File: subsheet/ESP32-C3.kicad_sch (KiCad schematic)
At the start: 0 parts

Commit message: Add ESP32-C3 subsheet. SMall corrections
Add and wire up ESP32-C3-Mini on a subsheet, and note down which pins
are used for strapping etc. This will then be replaced with a bare-chip
ESP32-C3 circuit, much like with the existing ESP32-S3 circuit.
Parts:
- added C601: 100nF/50V, Capacitor_SMD:C_0603_1608Metric, symbol Device:C_Small
- added J601: Conn_01x06, Connector_PinSocket_2.54mm:PinSocket_1x06_P2.54mm_Vertical, symbol Connector_Generic:Conn_01x06
- added R601: 10kΩ, Resistor_SMD:R_0603_1608Metric, symbol Device:R_US
- added R602, R603: 100kΩ, Resistor_SMD:R_0603_1608Metric, symbol Device:R_Small_US
- added SW601, SW602: SW_Push, Button_Switch_SMD_custom:SW_PUSHBUTTON_2PIN_SMD_3×4×2.0, symbol Switch:SW_Push
- added U601: ESP32-C3-MINI-1, Espressif:ESP32-C3-MINI-1, symbol Espressif:ESP32-C3-MINI-1
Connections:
- new net +3V3: J601.4 (Pin_4), R601.1, R602.1, R603.1
- new net ESP_EN: C601.1, J601.5 (Pin_5), R601.2, SW602.2, U601.8 (EN/CHIP_PU)
- new net GND: C601.2, J601.1 (Pin_1), SW601.1, SW602.1, U601.1 (GND), U601.11 (GND), U601.14 (GND), U601.2 (GND), U601.36 (GND), U601.37 (GND), U601.38 (GND), U601.39 (GND), U601.40 (GND), U601.41 (GND), U601.42 (GND), U601.43 (GND), U601.44 (GND), U601.45 (GND), U601.46 (GND), U601.47 (GND), U601.48 (GND), U601.49 (GND), U601.50 (GND), U601.51 (GND), U601.52 (GND), U601.53 (GND)
- new net GPIO18/USB_D-: U601.26 (GPIO18/USB_D-)
- new net GPIO19/USB_D+: U601.27 (GPIO19/USB_D+)
- new net GPIO43/UART0.Tx: J601.2 (Pin_2), U601.31 (GPIO21/U0TXD)
- new net GPIO44/UART0.Rx: J601.3 (Pin_3), U601.30 (GPIO20/U0RXD)
- new net IO0: U601.12 (GPIO0/ADC1_CH0/XTAL_32K_P)
- new net IO1: U601.13 (GPIO1/ADC1_CH1/XTAL_32K_N)
- new net IO10: U601.16 (GPIO10)
- new net IO2/STRAP^{PU}: R602.2, U601.5 (GPIO2/ADC1_CH2)
- new net IO3: U601.6 (GPIO3/ADC1_CH3)
- new net IO4: U601.18 (GPIO4/ADC1_CH4)
- new net IO5: U601.19 (GPIO5/ADC2_CH0)
- new net IO6: U601.20 (GPIO6)
- new net IO7: U601.21 (GPIO7)
- new net IO8/STRAP^{PU}: R603.2, U601.22 (GPIO8)
- new net IO9/BOOT^{PU}: J601.6 (Pin_6), SW601.2, U601.23 (GPIO9), U601.3 (3V3)
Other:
- note added: "Gnd Tx Rx 3v3 EN Boot"
- note added: "Some pins are used for bootstrapping, and thus they must have the correct state when booting: GPIO- state - reason 9 - FLOAT - Allows code to be downloaded - Has an internal pull-up 8 - HIGH/FLOAT - Download boot mode - Only checked if 9 is LOW 2 - HIGH/FLOAT - Prevents glitches - Not technically a strapping pin. ADC1 (5 channels) available on GPIO's 0-4 ADC2 on GPIO 5. Doesn't work? (see datashe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"
- note added: "This RC circuit is ESSENTIAL to the auto-programming circuits function."

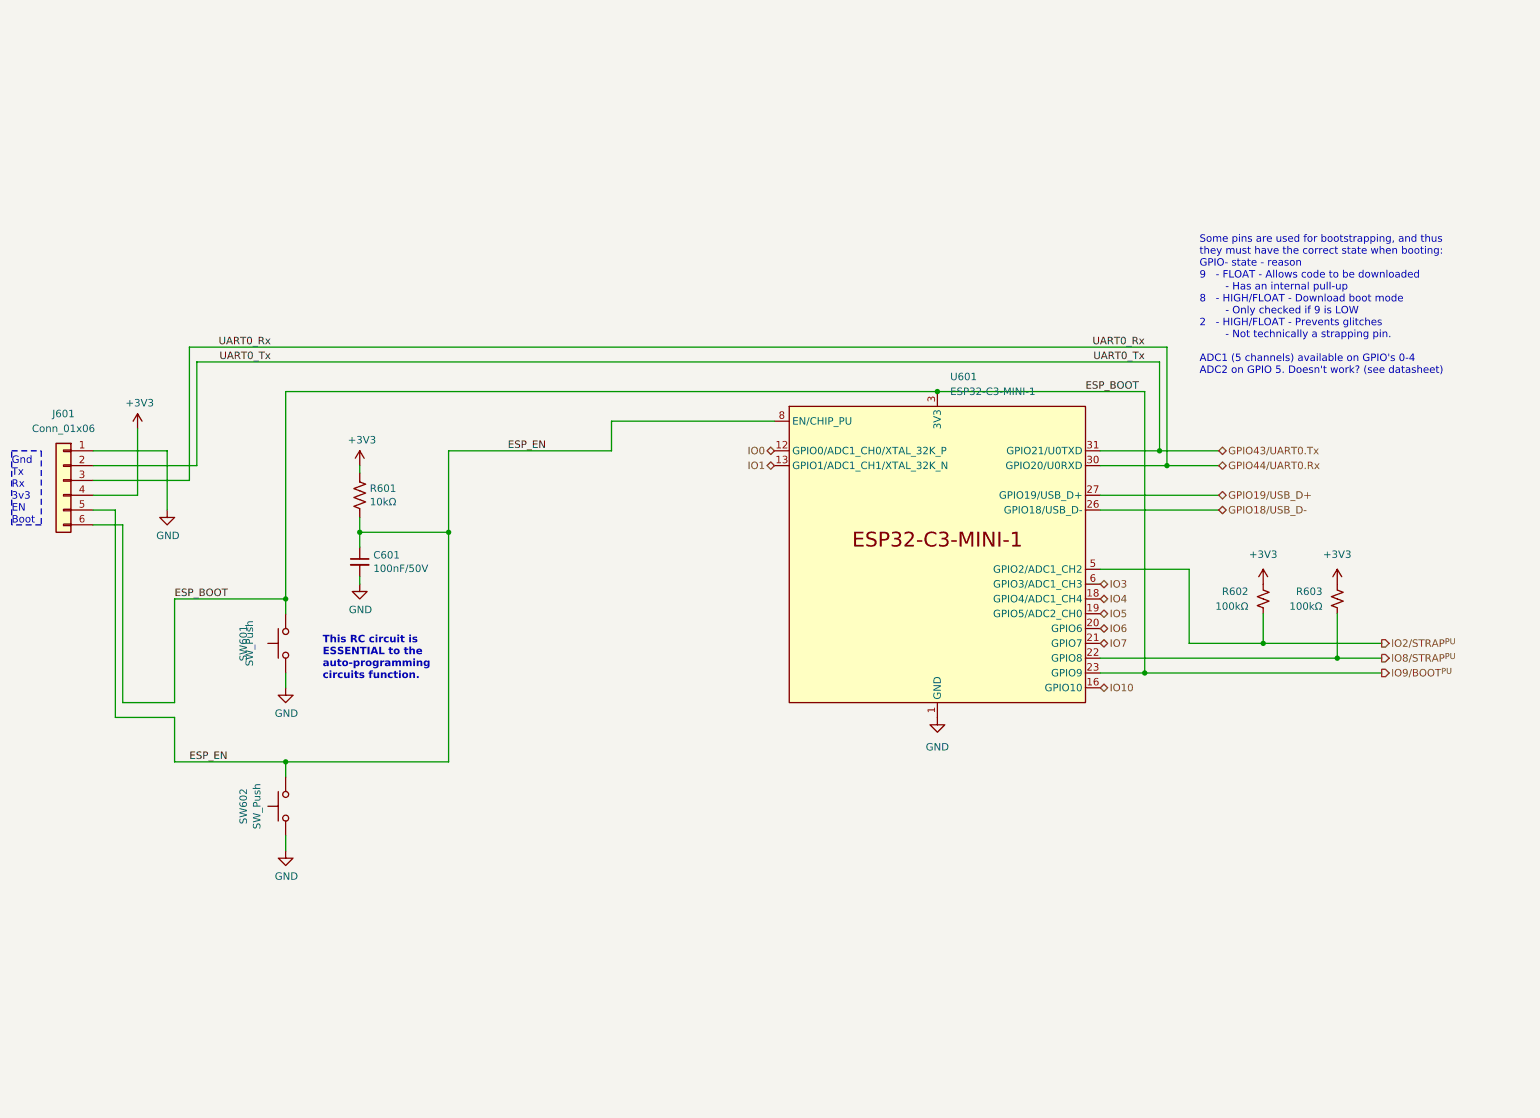
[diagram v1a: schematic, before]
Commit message: Add sheet for ESP32-C3 bare chip as well.
Similar to the ESP32-S3 circuit, so I copied most of it (one capacitor
is not needed, according to the reference schematics).

No flash chip is attached; makes sense to use one of the embedded flash
chips to test with, as it makes for a very small design (and 16MB is
really not needed).
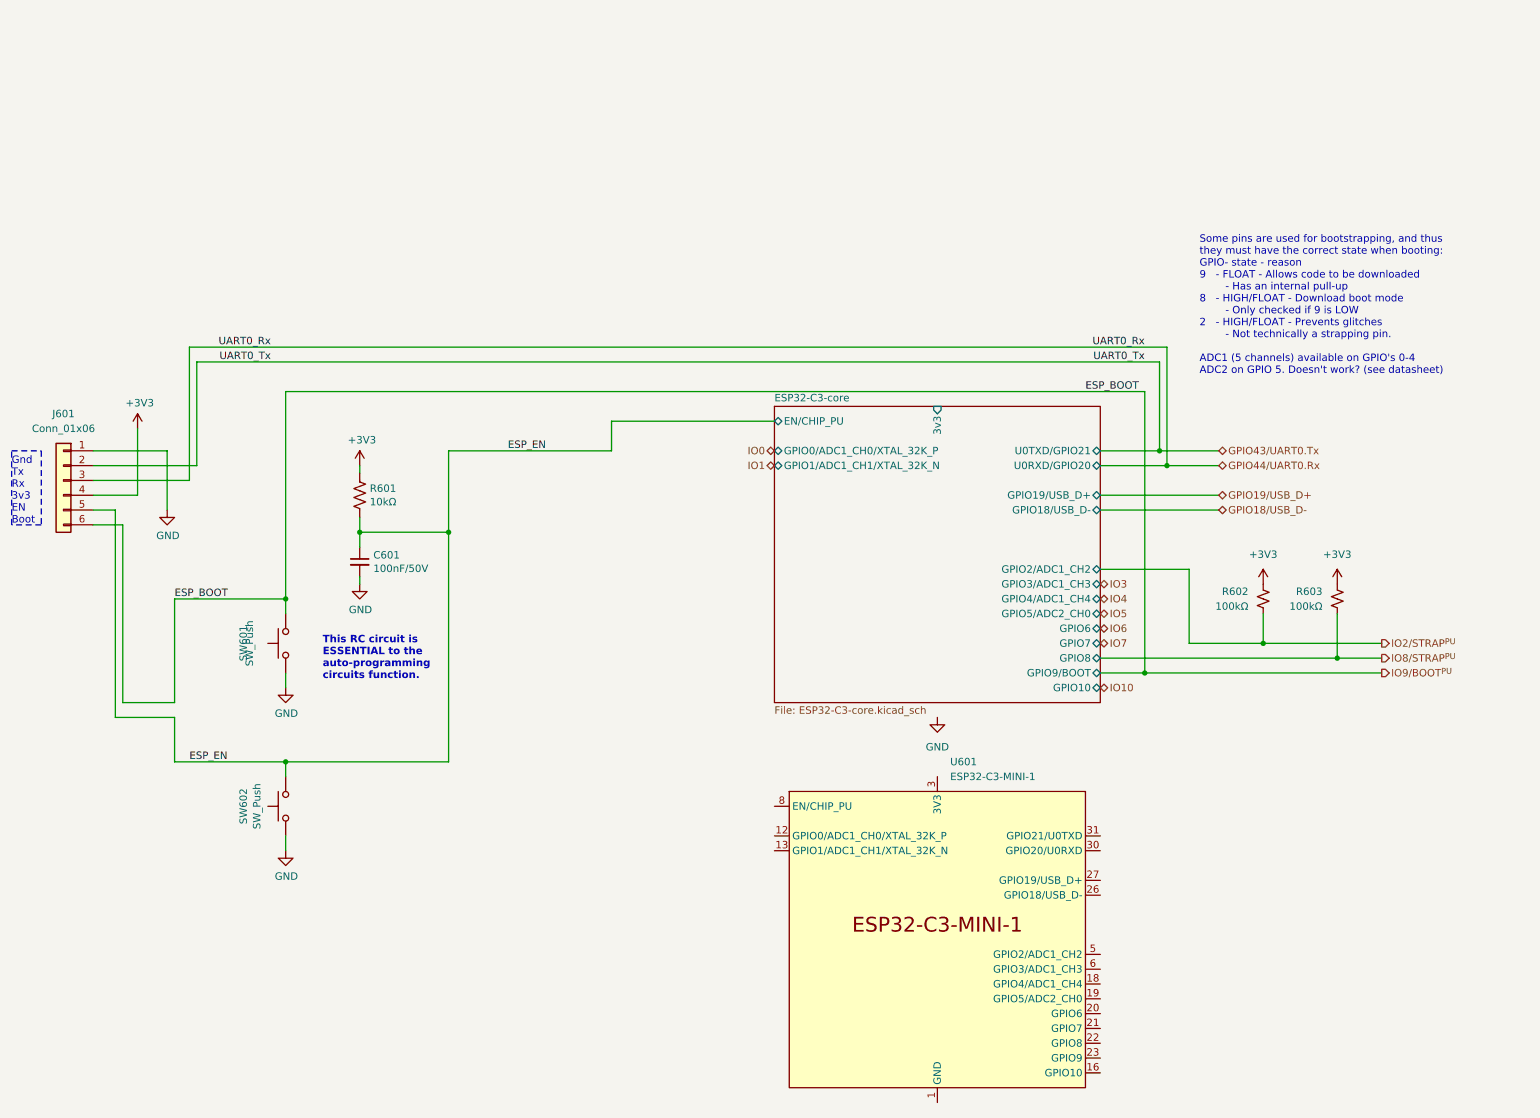
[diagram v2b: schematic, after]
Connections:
- net ESP_EN: no longer U601.8 (EN/CHIP_PU)
- net GND: no longer U601.1 (GND), U601.11 (GND), U601.14 (GND), U601.2 (GND), U601.36 (GND), U601.37 (GND), U601.38 (GND), U601.39 (GND), U601.40 (GND), U601.41 (GND), U601.42 (GND), U601.43 (GND), U601.44 (GND), U601.45 (GND), U601.46 (GND), U601.47 (GND), U601.48 (GND), U601.49 (GND), U601.50 (GND), U601.51 (GND), U601.52 (GND), U601.53 (GND)
- net GPIO18/USB_D-: no longer U601.26 (GPIO18/USB_D-)
- net GPIO19/USB_D+: no longer U601.27 (GPIO19/USB_D+)
- net GPIO43/UART0.Tx: no longer U601.31 (GPIO21/U0TXD)
- net GPIO44/UART0.Rx: no longer U601.30 (GPIO20/U0RXD)
- net IO0: no longer U601.12 (GPIO0/ADC1_CH0/XTAL_32K_P)
- net IO1: no longer U601.13 (GPIO1/ADC1_CH1/XTAL_32K_N)
- net IO10: no longer U601.16 (GPIO10)
- net IO2/STRAP^{PU}: no longer U601.5 (GPIO2/ADC1_CH2)
- net IO3: no longer U601.6 (GPIO3/ADC1_CH3)
- net IO4: no longer U601.18 (GPIO4/ADC1_CH4)
- net IO5: no longer U601.19 (GPIO5/ADC2_CH0)
- net IO6: no longer U601.20 (GPIO6)
- net IO7: no longer U601.21 (GPIO7)
- net IO8/STRAP^{PU}: no longer U601.22 (GPIO8)
- net IO9/BOOT^{PU}: no longer U601.23 (GPIO9), U601.3 (3V3)
- new net: U601.1 (GND), U601.11 (GND), U601.14 (GND), U601.2 (GND), U601.36 (GND), U601.37 (GND), U601.38 (GND), U601.39 (GND), U601.40 (GND), U601.41 (GND), U601.42 (GND), U601.43 (GND), U601.44 (GND), U601.45 (GND), U601.46 (GND), U601.47 (GND), U601.48 (GND), U601.49 (GND), U601.50 (GND), U601.51 (GND), U601.52 (GND), U601.53 (GND)
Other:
- added sheet ESP32-C3-core (ESP32-C3-core.kicad_sch)
- moved on the sheet: U601
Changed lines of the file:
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@@
-	)
-	(junction
-		(at 172.72 83.82)
-		(diameter 0)
-		(color 0 0 0 0)
 	)
 	(junction
@@
 	(wire
 		(pts
-			(xy 172.72 83.82) (xy 208.28 83.82)
-		)
-		(stroke
-			(width 0)
-			(type solid)
-		)
-	)
-	(wire
-		(pts
 			(xy 73.66 107.95) (xy 73.66 110.49)
 		)
@@
 	(wire
 		(pts
-			(xy 60.96 83.82) (xy 172.72 83.82)
+			(xy 60.96 83.82) (xy 208.28 83.82)
 		)
 		(stroke
@@
 	(symbol
 		(lib_id "Espressif:ESP32-C3-MINI-1")
-		(at 172.72 111.76 0)
+		(at 172.72 177.8 0)
 		(unit 1)
 		(exclude_from_sim no)
@@
 		(fields_autoplaced yes)
 		(property "Reference" "U601"
-			(at 174.9141 81.28 0)
+			(at 174.9141 147.32 0)
 			(effects
 				(font
@@
 		)
 		(property "Value" "ESP32-C3-MINI-1"
-			(at 174.9141 83.82 0)
+			(at 174.9141 149.86 0)
 			(effects
 				(font
@@
 		)
 		(property "Footprint" "Espressif:ESP32-C3-MINI-1"
-			(at 172.72 147.32 0)
+			(at 172.72 213.36 0)
 			(effects
 				(font
@@
 		)
 		(property "Datasheet" "https://www.espressif.com/sites/default/files/documentation/esp32-c3-mini-1_datasheet_en.pdf"
-			(at 172.72 149.86 0)
+			(at 172.72 215.9 0)
 			(effects
 				(font
@@
 		)
 		(property "Description" "ESP32-C3-MINI-1 family is an ultra-low-power MCU-based SoC solution that supports 2.4 GHz Wi-Fi and Bluetooth®Low Energy (Bluetooth LE)."
-			(at 172.72 111.76 0)
+			(at 172.72 177.8 0)
 			(effects
 				(font
@@
 				)
 			)
+		)
+	)
+	(sheet
+		(at 144.78 86.36)
+		(size 55.88 50.8)
+		(fields_autoplaced yes)
+		(stroke
+			(width 0.1524)
+			(type solid)
+		)
+		(fill
+			(color 255 229 191 1.0000)
+		)
+		(property "Sheetname" "ESP32-C3-core"
+			(at 144.78 85.6484 0)
+			(effects
+				(font
+					(size 1.27 1.27)
+				)
+				(justify left bottom)
+			)
+		)
+		(property "Sheetfile" "ESP32-C3-core.kicad_sch"
+			(at 144.78 137.7446 0)
+			(effects
+				(font
+					(size 1.27 1.27)
+				)
+				(justify left top)
+			)
+		)
+		(pin "GPIO7" bidirectional
+			(at 200.66 127 0)
+			(effects
+				(font
+					(size 1.27 1.27)
+				)
+				(justify right)
+			)
+		)
+		(pin "3v3" input
+			(at 172.72 86.36 90)
+			(effects
+				(font
+					(size 1.27 1.27)
+				)
+				(justify right)
+			)
+		)
+		(pin "GPIO0{slash}ADC1_CH0{slash}XTAL_32K_P" bidirectional
+			(at 144.78 93.98 180)
+			(effects
+				(font
+					(size 1.27 1.27)
+				)
+				(justify left)
+			)
+		)
+		(pin "GPIO1{slash}ADC1_CH1{slash}XTAL_32K_N" bidirectional
+			(at 144.78 96.52 180)
+			(effects
+				(font
+					(size 1.27 1.27)
+				)
+				(justify left)
+			)
+		)
+		(pin "EN{slash}CHIP_PU" bidirectional
+			(at 144.78 88.9 180)
+			(effects
+				(font
+					(size 1.27 1.27)
+				)
+				(justify left)
+			)
+		)
+		(pin "GPIO4{slash}ADC1_CH4" bidirectional
+			(at 200.66 119.38 0)
+			(effects
+				(font
+					(size 1.27 1.27)
+				)
+				(justify right)
+			)
+		)
+		(pin "GPIO5{slash}ADC2_CH0" bidirectional
+			(at 200.66 121.92 0)
+			(effects
+				(font
+					(size 1.27 1.27)
+				)
+				(justify right)
+			)
+		)
+		(pin "GPIO6" bidirectional
+			(at 200.66 124.46 0)
+			(effects
+				(font
+					(size 1.27 1.27)
+				)
+				(justify right)
+			)
+		)
+		(pin "GPIO18{slash}USB_D-" bidirectional
+			(at 200.66 104.14 0)
+			(effects
+				(font
+					(size 1.27 1.27)
+				)
+				(justify right)
+			)
+		)
+		(pin "U0RXD{slash}GPIO20" bidirectional
+			(at 200.66 96.52 0)
+			(effects
+				(font
+					(size 1.27 1.27)
+				)
+				(justify right)
+			)
+		)
+		(pin "GPIO19{slash}USB_D+" bidirectional
+			(at 200.66 101.6 0)
+			(effects
+				(font
+					(size 1.27 1.27)
+				)
+				(justify right)
+			)
+		)
+		(pin "U0TXD{slash}GPIO21" bidirectional
+			(at 200.66 93.98 0)
+			(effects
+				(font
+					(size 1.27 1.27)
+				)
+				(justify right)
+			)
+		)
+		(pin "GPIO10" bidirectional
+			(at 200.66 134.62 0)
+			(effects
+				(font
+					(size 1.27 1.27)
+				)
+				(justify right)
+			)
+		)
+		(pin "GPIO3{slash}ADC1_CH3" bidirectional
+			(at 200.66 116.84 0)
+			(effects
+				(font
+					(size 1.27 1.27)
+				)
+				(justify right)
+			)
+		)
+		(pin "GPIO9{slash}BOOT" bidirectional
+			(at 200.66 132.08 0)
+			(effects
+				(font
+					(size 1.27 1.27)
+				)
+				(justify right)
+			)
+		)
+		(pin "GPIO2{slash}ADC1_CH2" bidirectional
+			(at 200.66 114.3 0)
+			(effects
+				(font
+					(size 1.27 1.27)
+				)
+				(justify right)
+			)
+		)
+		(pin "GPIO8" bidirectional
+			(at 200.66 129.54 0)
+			(effects
+				(font
+					(size 1.27 1.27)
+				)
+				(justify right)
+			)
+		)
+		(instances
+			(project "ESP_bare_chip_test_board"
+				(path "/45b6f84a-e69b-48be-a49b-bc68872e2c15/01bb46e3-d129-4909-82a1-6bb013dc8f71"
+					(page "7")
+				)
+			)

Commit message: PCB changes, added useful connectors
Added a whole bunch of things that should make it useful - e.g.
ethernet, an extra flash chip for general storage, piicodev connectors
for I2C.

Also added a GPIB connector footprint; dev-board version worked nicely,
but may as well make this work for that too. Saves bying dev boards : )
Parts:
- added C602: 100nF/50V, Capacitor_SMD:C_0603_1608Metric, symbol Device:C_Small
- added C603: 22uF/6.3V, Capacitor_SMD:C_0603_1608Metric, symbol Device:C_Small
- U601: now not fitted; now left out of the parts list
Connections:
- net GND: now also C602.2, C603.2
- net GPIO43/UART0.Tx renamed GPIO21/UART0.Tx
- net GPIO44/UART0.Rx renamed GPIO20/UART0.Rx
- new net 3v3_{AUX}: C602.1, C603.1
